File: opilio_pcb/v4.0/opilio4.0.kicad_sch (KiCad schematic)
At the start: 79 parts, among them J1 Screw_Terminal_01x02, J2 Conn_01x02_Male, J3 USB_B_Micro, J4 Program, J5 Conn_01x02_Male, Q1 SI2306_C427393, Q2 SI2306_C427393, U1 AMS1117-3.3, U4 USBLC6-2SC6, U5 STM32F103C8T6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

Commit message: v4 almost ready
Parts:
- removed C28: 220uF, Capacitor_SMD:CP_Elec_6.3x7.7, symbol Device:C_Small
- removed D1, D4: B230A-13-F, Diode_SMD:D_SMA, symbol Device:D_Schottky_Small
- removed D10, D3, D8, D9: B5819W, Diode_SMD:D_SOD-123, symbol Device:D_Schottky_Small
- removed FAN_S1: F_EN, easyedakicad:SW-SMD_L6.0-W3.3-LS8.0, symbol Switch:SW_Push
- removed PUMP_S1: P_EN, easyedakicad:SW-SMD_L6.0-W3.3-LS8.0, symbol Switch:SW_Push
- removed Q1, Q2: SI2306_C427393, Package_TO_SOT_SMD:SOT-23, symbol easyeda:SI2306_C427393
- added BUZZER1: HNB09A03, easyeda2kicad:BUZ-TH_BD9.0-P5.00-D0.6-FD, symbol easyeda:HNB09A03
- added C3: 10uF, Capacitor_SMD:C_0603_1608Metric_Pad1.08x0.95mm_HandSolder, symbol Device:C_Small
- added C4: 22uF, Capacitor_SMD:C_1206_3216Metric_Pad1.33x1.80mm_HandSolder, symbol Device:C_Small
- added C7: 100nF, Capacitor_SMD:C_0603_1608Metric_Pad1.08x0.95mm_HandSolder, symbol Device:C_Small
- added D1, D3: B230, Diode_SMD:D_SMB, symbol Diode:B230
- added Q1, Q2: PMV25ENEAR, easyeda2kicad:SOT-23_L2.9-W1.3-P1.90-LS2.4-BR, symbol easyeda:PMV25ENEAR
- added R18, R7: 0R, Resistor_SMD:R_0603_1608Metric_Pad0.98x0.95mm_HandSolder, symbol Device:R_Small
- added R2: 100R, Resistor_SMD:R_0603_1608Metric_Pad0.98x0.95mm_HandSolder, symbol Device:R_Small
- added R4, R5: 10K, Resistor_SMD:R_0603_1608Metric_Pad0.98x0.95mm_HandSolder, symbol Device:R_Small
- J4: footprint Connector_PinHeader_2.54mm:PinHeader_1x04_P2.54mm_Vertical -> Connector_PinHeader_2.54mm:PinHeader_1x05_P2.54mm_Vertical; symbol Connector_Generic:Conn_01x04 -> Connector_Generic:Conn_01x05
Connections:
- net +12V: now also F1.1
- net +12VF(F): now also D3.1 (K)
- net +12VF(P): now also D1.1 (K)
- net +3.3V: now also J4.5 (Pin_5), C3.1; no longer J4.4 (Pin_4)
- net FAN_EN: now also R7.1
- net GND: now also BUZZER1.2 (-), C3.2, C4.2, C7.2, Q1.2 (S), Q2.2 (S), R4.1, R5.1
- net PUMP_EN: now also R18.1
- net PWM_OUT1: now also D2.1 (K); no longer D2.2 (K)
- net PWM_OUT2: now also D5.1 (K); no longer D5.2 (K)
- net PWM_OUT3: now also D6.1 (K); no longer D6.2 (K)
- net PWM_READ1: now also D2.2 (K); no longer D2.1 (K)
- net PWM_READ2: now also D5.2 (K); no longer D5.1 (K)
- net PWM_READ3: now also D6.2 (K); no longer D6.1 (K)
- net SWCLK: now also J4.3 (Pin_3); no longer J4.2 (Pin_2)
- net SWIO: now also J4.4 (Pin_4); no longer J4.3 (Pin_3)
- net BUZZER: now reaches U5.22 (PB11)
- net BUZZER: now also R2.1
- net at F1.2, FB1.2: now also C4.1
- net FAN_GND renamed F_GND
- net F_GND: now also D3.2 (A), Q1.3 (D)
- net PUMP_GND renamed P_GND
- net P_GND: now also D1.2 (A), Q2.3 (D)
- new net: Q1.1 (G), R4.2, R7.2
- new net: BUZZER1.1 (+), C7.1, R2.2
- new net: Q2.1 (G), R18.2, R5.2
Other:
- title: Opilio 3.2 -> Opilio
- moved on the sheet: C16, C17, C2, C23, C24, C9, F1, F2, F3, FAN1, FAN2, FAN3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

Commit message: ordered
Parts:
- D4: renamed from U4; footprint Package_TO_SOT_SMD:SOT-23-6 -> easyeda2kicad:SOT-666-6_L1.6-W1.2-P0.50-LS1.6-BL; symbol Power_Protection:USBLC6-2SC6 -> easyeda:USBLC6-2P6_C2827693; JLC Part (none) -> Extended Part; LCSC Part (none) -> C2827693; Manufacturer (none) -> TECH PUBLIC(台舟)
- J1: footprint Custom:TerminalBlock_bornier-2_P5.08mm -> easyeda2kicad:CONN-TH_2P-P2.54_JL300-50002U01; symbol Connector:Screw_Terminal_01x02 -> easyeda:JL300-50002U01; JLC Part (none) -> Extended Part; LCSC Part (none) -> C387831; Manufacturer (none) -> JILN
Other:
- moved on the sheet: BL1, BUZZER1, C13, C14, C7, J3, L2, Power1, R12, R16, R17, R2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

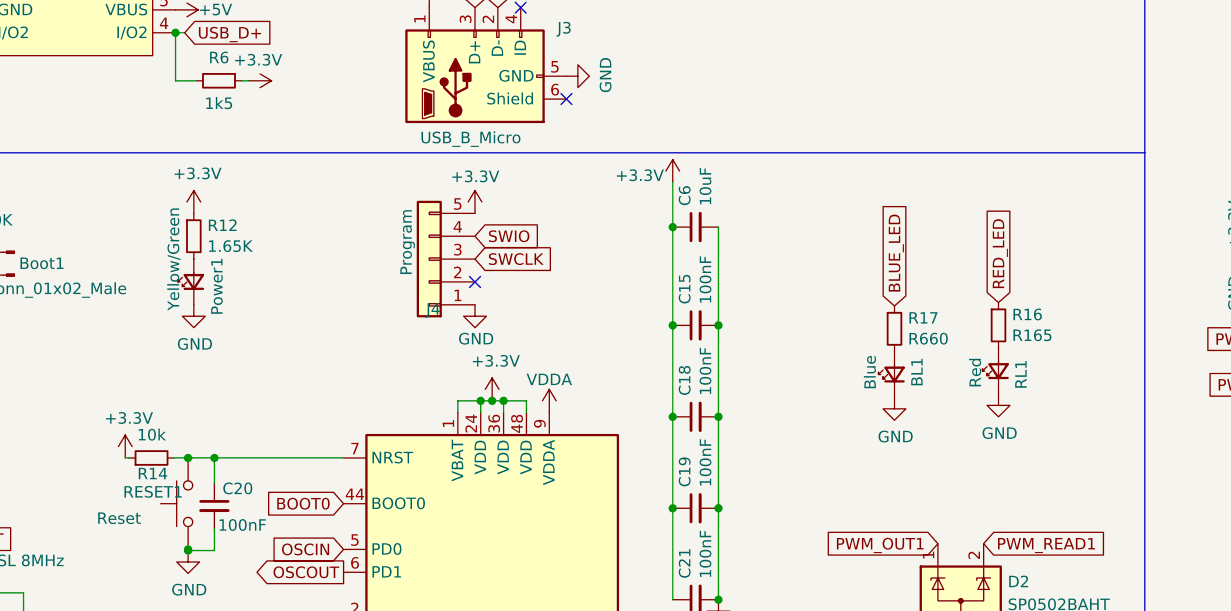
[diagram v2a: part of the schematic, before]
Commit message: add tag-connect
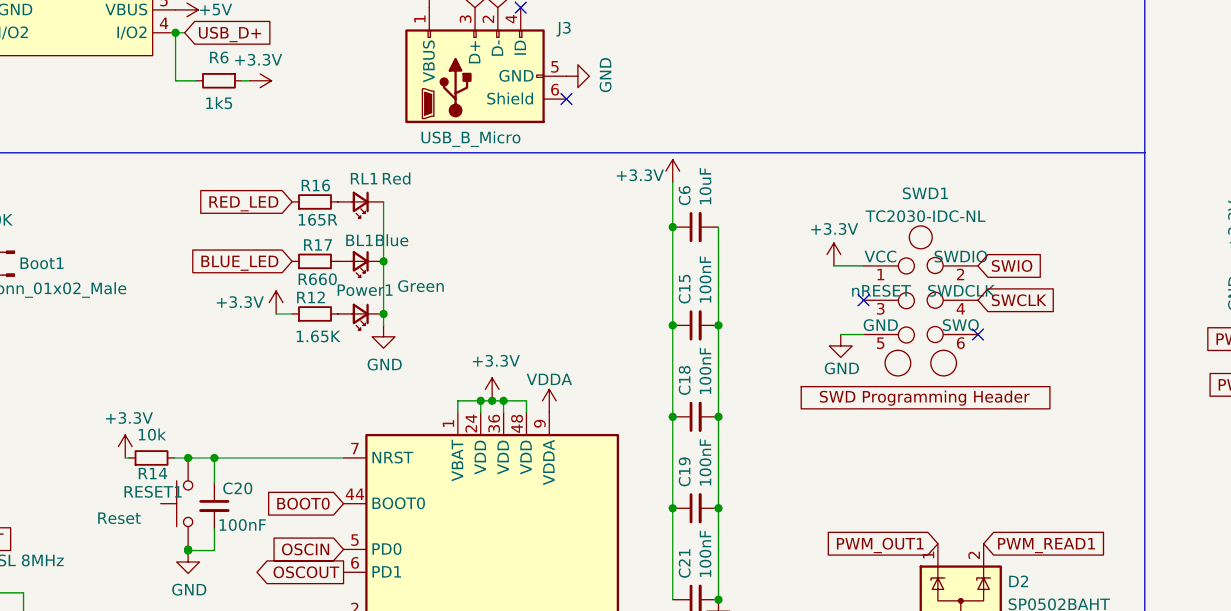
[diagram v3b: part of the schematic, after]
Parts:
- removed J4: Program, Connector_PinHeader_2.54mm:PinHeader_1x05_P2.54mm_Vertical, symbol Connector_Generic:Conn_01x05
- added SWD1: TC2030-IDC-NL_SWD, tag_connect:Tag-Connect_TC2030-IDC-NL_2x03_P1.27mm_Vertical, symbol tag_connect:TC2030-IDC-NL_SWD
- Power1: value Yellow/Green -> Green
- R16: value R165 -> 165R
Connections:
- net +3.3V: now also SWD1.1 (VCC)
- net GND: now also SWD1.5 (GND)
- net SWCLK: now also SWD1.4 (SWDCLK)
- net SWIO: now also SWD1.2 (SWDIO)
- no-connect marks 19 -> 20
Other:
- moved on the sheet: BL1, Power1, R12, R16, R17, RL1

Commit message: update schema files
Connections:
- net NRST: now reaches C20.1, R14.2, RESET1.2, U5.7 (NRST)
- net NRST: now also SWD1.3 (nRESET)
- no-connect marks 20 -> 19
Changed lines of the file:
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@@
   (no_connect (at 104.013 169.672))
   (no_connect (at 70.993 151.892))
-  (no_connect (at 128.778 101.346))
   (no_connect (at 141.478 105.156))
   (no_connect (at 265.43 143.51))
@@
     (stroke (width 0) (type default) (color 0 0 0 0))
   )
+  (wire (pts (xy 56.642 117.856) (xy 56.642 118.872))
+    (stroke (width 0) (type default) (color 0 0 0 0))
+  )
   (wire (pts (xy 264.287 104.902) (xy 262.636 104.902))
     (stroke (width 0) (type default) (color 0 0 0 0))
@@
     (property "Intersheet References" "${INTERSHEET_REFS}" (id 0) (at 249.3553 109.9026 0)
       (effects (font (size 1.27 1.27)) (justify right) hide)
+    )
+  )
+  (global_label "NRST" (shape input) (at 56.642 117.856 90) (fields_autoplaced)
+    (effects (font (size 1.27 1.27)) (justify left))
+    (property "Intersheet References" "${INTERSHEET_REFS}" (id 0) (at 56.7214 110.6653 90)
+      (effects (font (size 1.27 1.27)) (justify left) hide)
     )
   )
@@
       (effects (font (size 1.27 1.27)) (justify right) hide)
     )
+  )
+  (global_label "NRST" (shape input) (at 128.778 101.346 180) (fields_autoplaced)
+    (effects (font (size 1.27 1.27)) (justify right))
+    (property "Intersheet References" "${INTERSHEET_REFS}" (id 0) (at 121.5873 101.2666 0)
+      (effects (font (size 1.27 1.27)) (justify right) hide)
+    )
